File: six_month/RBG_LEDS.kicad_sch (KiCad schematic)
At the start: 35 parts, among them Q1 SI2302_C4748714, U5 SN74LV1T34DCK

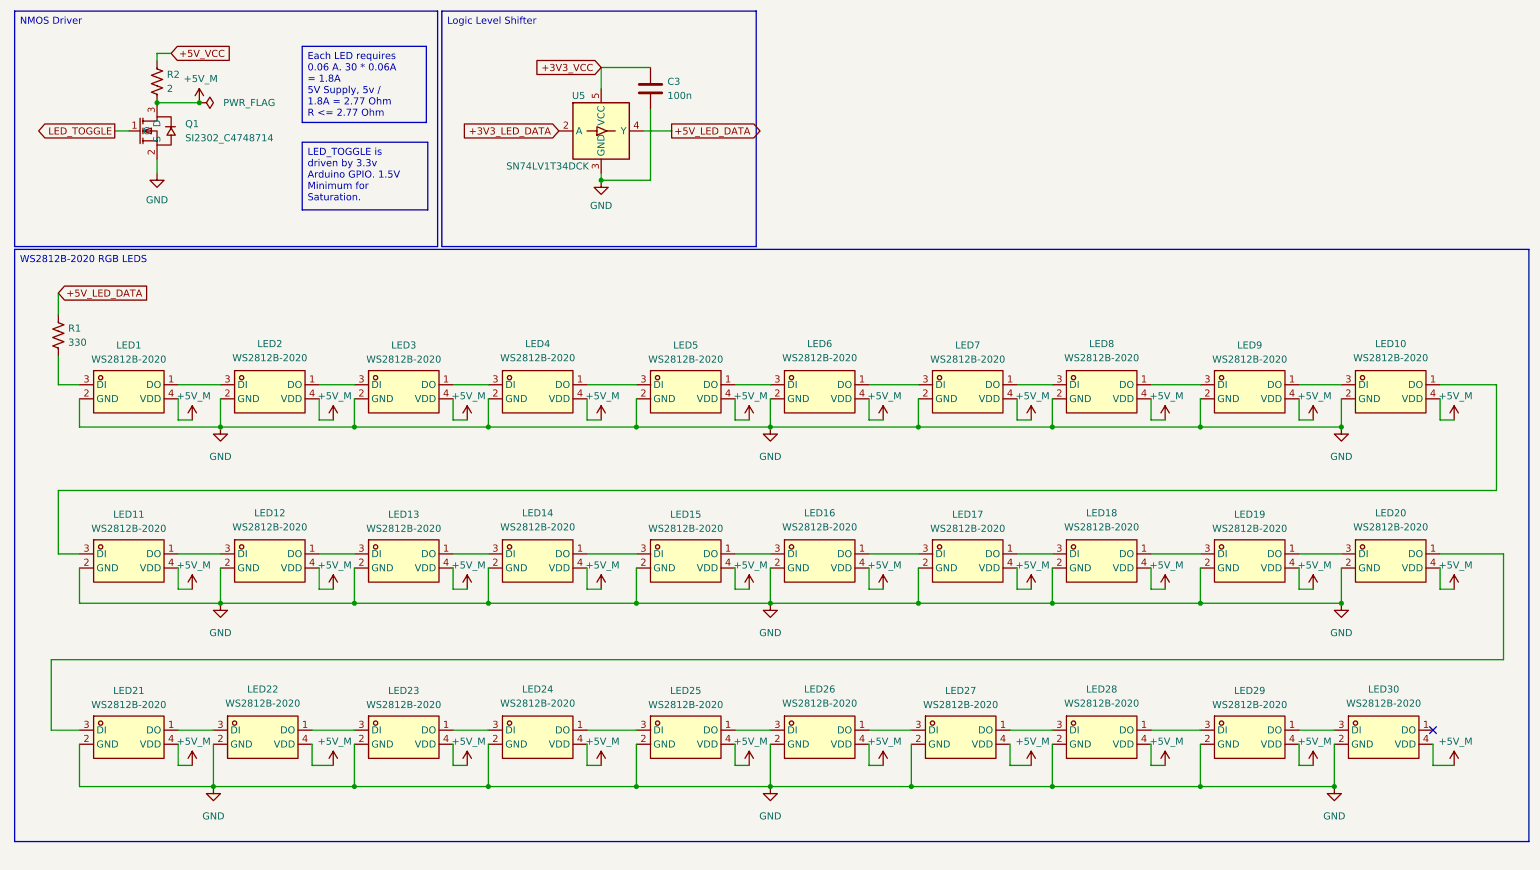
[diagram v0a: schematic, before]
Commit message: Changes
Removed the microphone idea, added a DAC for Bluetooth to Line out. Allows for external speakers to be connected via an Aux cable
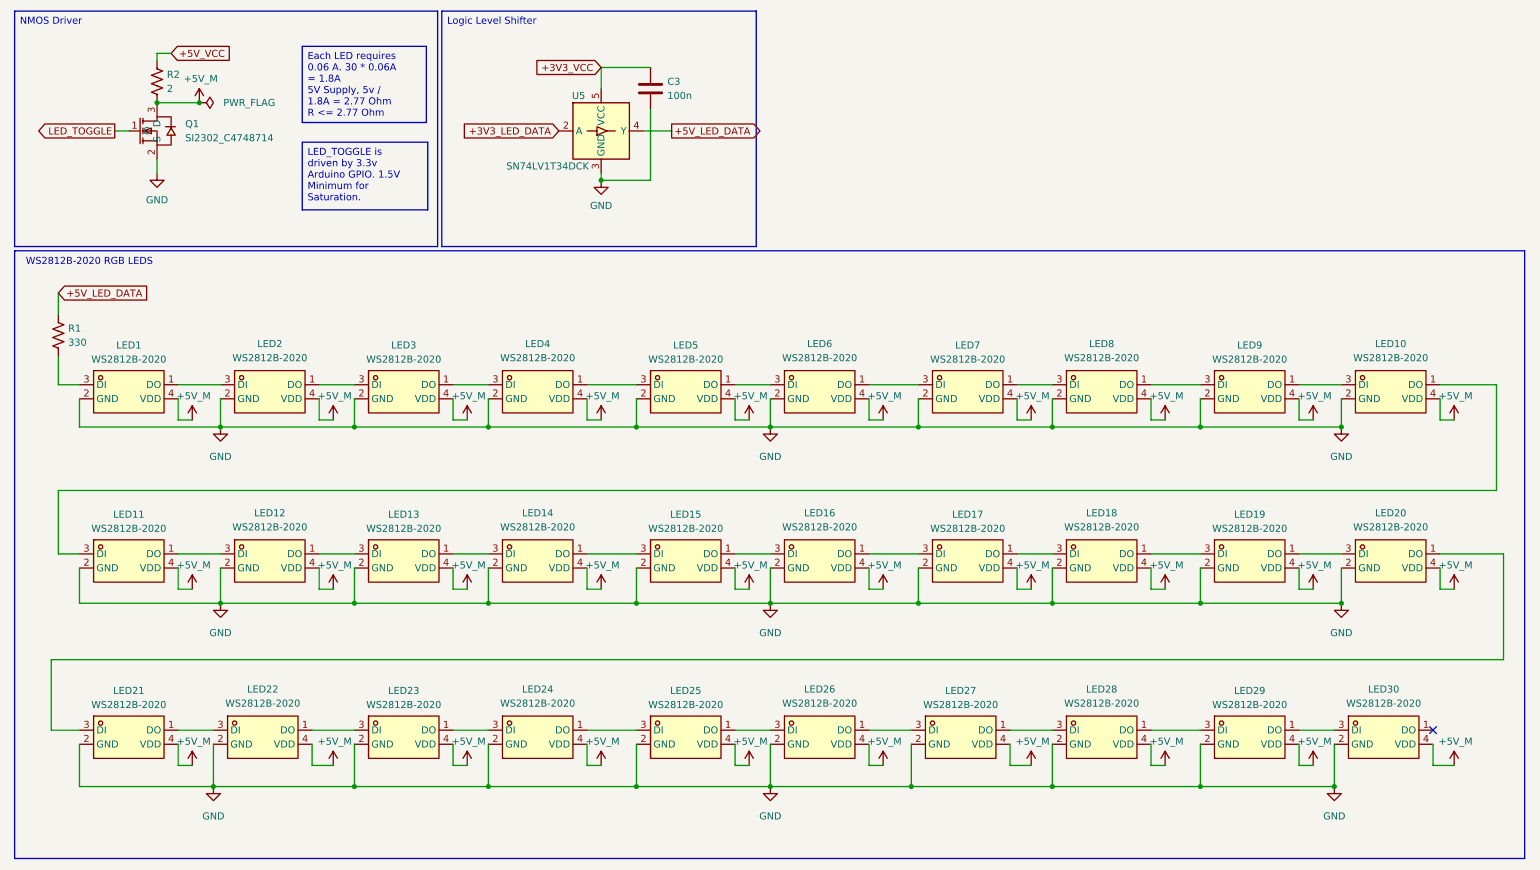
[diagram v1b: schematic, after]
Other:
- note added: "WS2812B-2020 RGB LEDS"
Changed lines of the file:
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@@
 	(generator_version "9.0")
 	(paper "A4")
+	(rectangle
+		(start 12.446 55.88)
+		(end 284.48 165.354)
+		(stroke
+			(width 0)
+			(type default)
+		)
+		(fill
+			(type none)
+		)
+	)
+	(text "WS2812B-2020 RGB LEDS"
+		(exclude_from_sim no)
+		(at 25.908 57.912 0)
+		(effects
+			(font
+				(size 1.27 1.27)
+			)
+		)
+	)
 	(text_box "NMOS Driver"
 		(exclude_from_sim no)
@@
 		(margins 0.9525 0.9525 0.9525 0.9525)
 		(stroke
-			(width 0)
-			(type solid)
-		)
-		(fill
-			(type none)
-		)
-		(effects
-			(font
-				(size 1.27 1.27)
-			)
-			(justify left top)
-		)
-	)
-	(text_box "WS2812B-2020 RGB LEDS"
-		(exclude_from_sim no)
-		(at 12.446 55.626 0)
-		(size 272.796 106.68)
-		(margins 0.9525 0.9525 0.9525 0.9525)
-		(stroke
